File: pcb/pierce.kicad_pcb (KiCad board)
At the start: 2 copper layers, 227.3 x 105.6 mm, 92 parts, among them J1 Conn_01x12, J2 Conn_01x12, J3 Trackpoint, SW1 SW_PUSH, SW10 SW_PUSH, SW11 SW_PUSH, SW12 SW_PUSH, SW13 SW_PUSH, SW14 SW_PUSH, SW15 SW_PUSH, SW16 SW_PUSH, SW17 SW_PUSH, SW18 SW_PUSH, SW19 SW_PUSH, SW2 SW_PUSH, SW20 SW_PUSH, SW21 SW_PUSH, SW22 SW_PUSH, SW23 SW_PUSH, SW24 SW_PUSH, SW25 SW_PUSH, SW26 SW_PUSH, SW27 SW_PUSH, SW28 SW_PUSH, SW29 SW_PUSH, SW3 SW_PUSH, SW30 SW_PUSH, SW31 SW_PUSH, SW32 SW_PUSH, SW33 SW_PUSH, SW34 SW_PUSH, SW35 SW_PUSH, SW36 SW_PUSH, SW37 SW_PUSH, SW38 Rotary_Encoder, SW4 SW_PUSH, SW5 SW_PUSH, SW6 SW_PUSH, SW7 SW_PUSH, SW8 SW_PUSH, SW9 SW_PUSH, U1 Elite-C_reverse

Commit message: locked mounting holes
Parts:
- added Ref**: Val**, kbd:M2_Threads_v2, F.Cu at (149.5, 70.9)
- added Ref**: Val**, kbd:M2_Threads_v2, F.Cu at (162.6, 75.5)

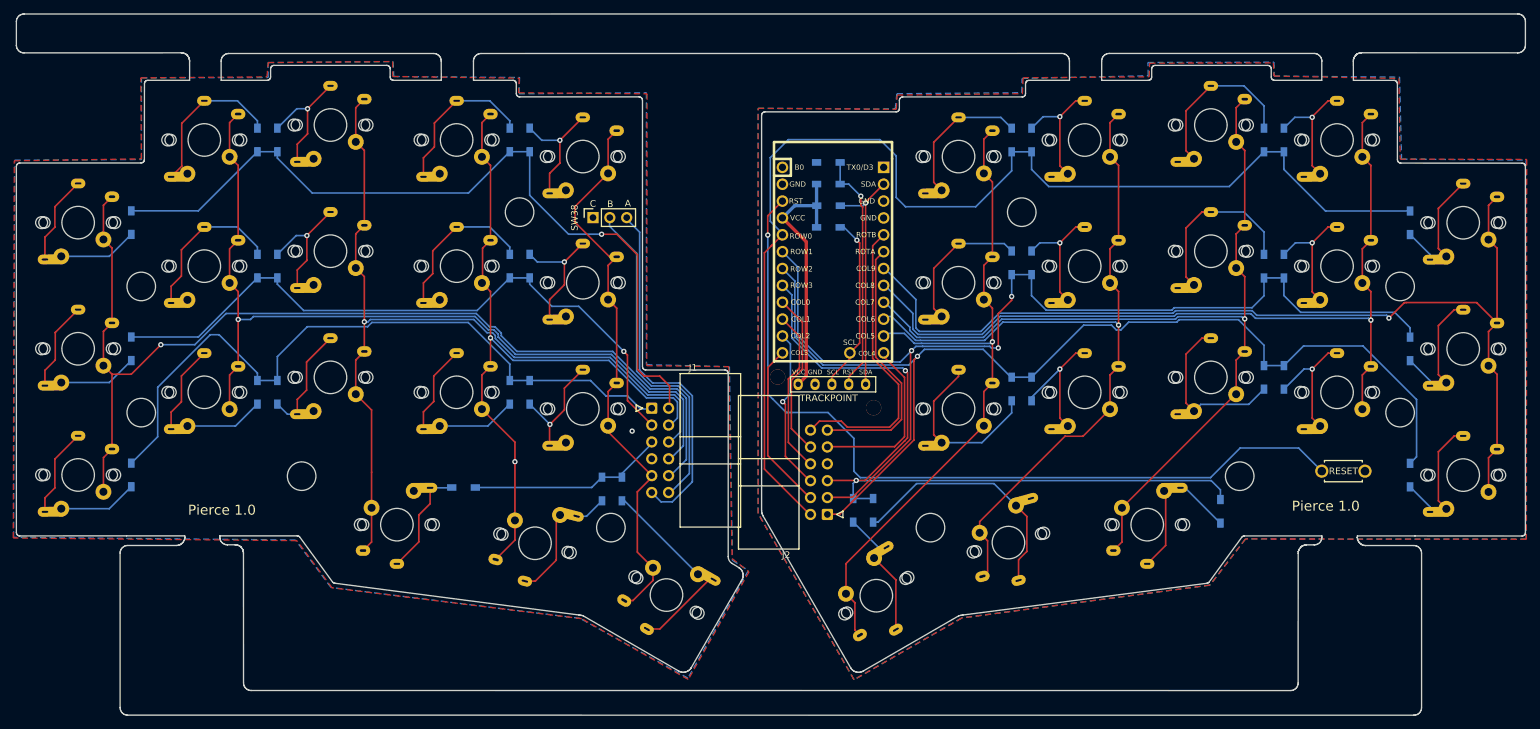
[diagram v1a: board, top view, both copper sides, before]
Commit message: changed switch footprint to support alps switcher
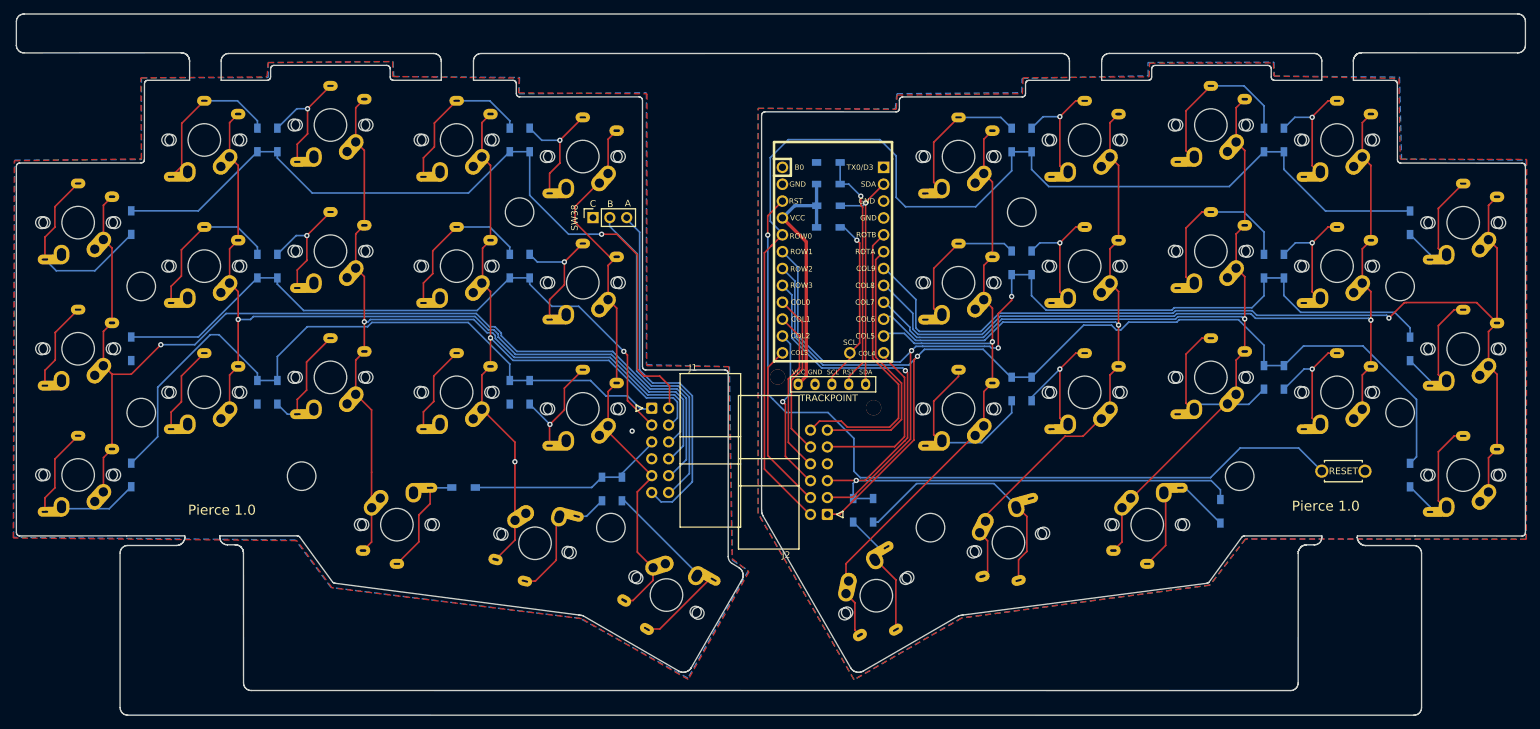
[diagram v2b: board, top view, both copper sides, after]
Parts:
- SW1, SW10, SW11, SW12, SW13, SW14, SW15, SW16, SW17, SW18, SW19, SW2, SW20, SW21, SW22, SW23, SW24, SW25, SW26, SW27, SW28, SW29, SW3, SW30, SW31, SW32, SW33, SW34, SW35, SW36, SW4, SW5, SW6, SW7, SW8, SW9: footprint kbd:CherryMX_ChocV2_1u -> kbd:keyswitch_cherrymx_alps_choc12_1u
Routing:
- net Net-(D25-Pad2): track 25.4 -> 13.5 mm
- net Net-(D2-Pad2): track 25.4 -> 13.5 mm
- net Net-(D10-Pad2): track 25.4 -> 13.5 mm
- net Net-(D1-Pad2): track 25.4 -> 29.5 mm

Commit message: adjust edgecut. add breakaway tabs
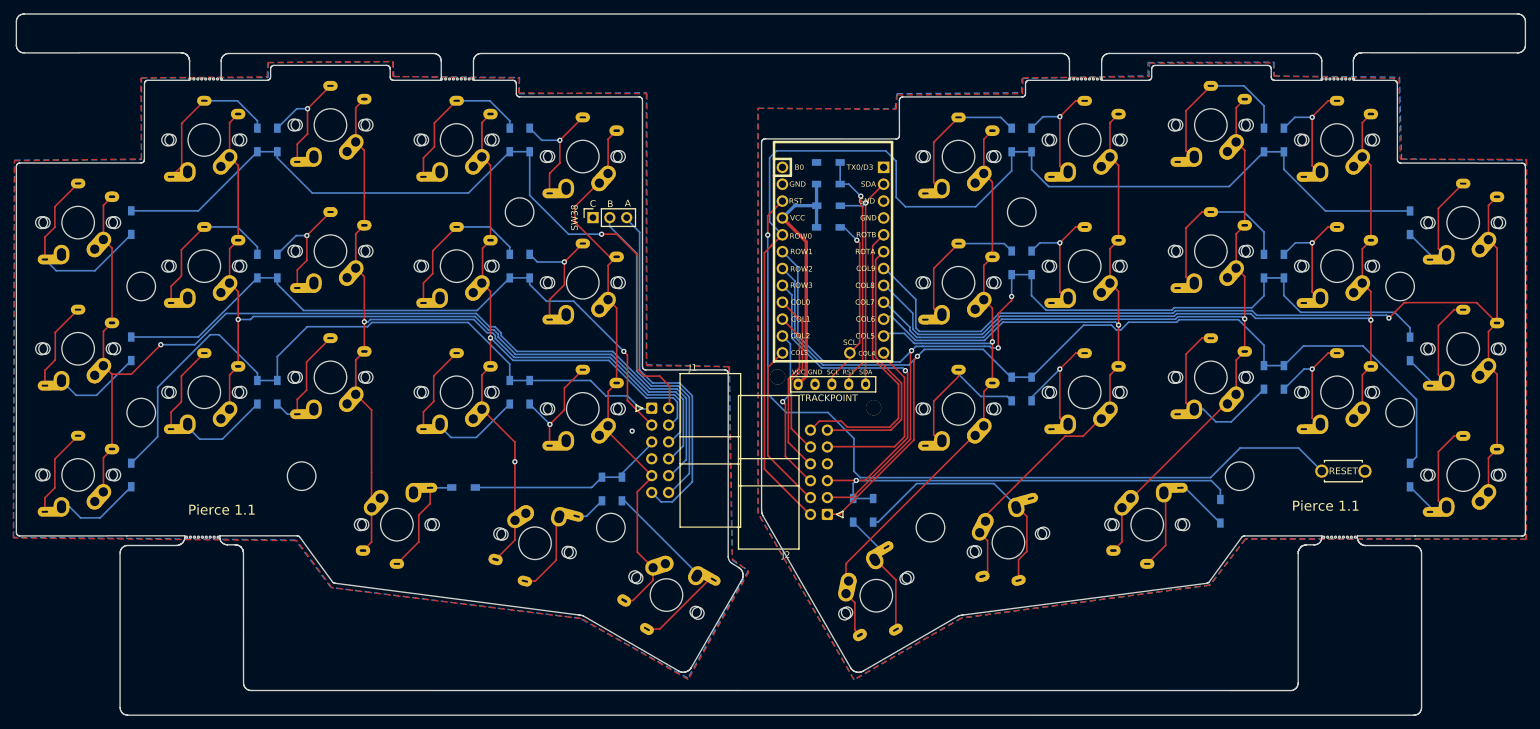
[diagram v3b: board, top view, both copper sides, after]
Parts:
- added REF**: Breakaway_Tabs, kbd:Breakaway_Tabs, F.Cu at (195.9, 26.0)
- added REF**: Breakaway_Tabs, kbd:Breakaway_Tabs, F.Cu at (233.9, 26.0)
- added REF**: Breakaway_Tabs, kbd:Breakaway_Tabs, F.Cu at (234.1, 95.0)
- added REF**: Breakaway_Tabs, kbd:Breakaway_Tabs, F.Cu at (62.9, 95.0)
- added REF**: Breakaway_Tabs, kbd:Breakaway_Tabs, F.Cu at (101.3, 26.0)
- added REF**: Breakaway_Tabs, kbd:Breakaway_Tabs, F.Cu at (63.4, 26.0)
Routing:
- net Net-(D10-Pad2): track 13.5 -> 27.4 mm
- net Net-(D25-Pad2): track 13.5 -> 27.1 mm
- net Net-(D2-Pad2): track 13.5 -> 27.1 mm
- net Net-(D6-Pad2): track 27.3 -> 23.4 mm
- net Net-(D21-Pad2): track 25.7 -> 28.6 mm
- net row0: track 179.7 -> 178.4 mm
- net Net-(D3-Pad2): track 25.4 -> 26.7 mm
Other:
- outline, holes or cut-outs redrawn
- board text added: "Pierce 1.1"
- board text removed: "Pierce 1.0"
